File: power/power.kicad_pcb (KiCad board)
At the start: 4 copper layers, 75 x 56 mm, 61 parts, among them J1 GPIO, J10 SCL1, J11 SDA1, J12 SCL2, J13 SDA2, J14 VCC1, J15 GND1, J16 VCC2, J17 GND2, J18 JP_VCC_PWM, J2 PWM_OUT, J3 PWM_IN, J4 JP_EXT, J5 JP_VOLTS, J6 I2C_EXT1, J7 I2C_EXT2, J8 PWM_OUT, J9 JP_VCC_PWM, Q1 D15P05, Q2 BC847C, U2 REF5050IDGK, U3 L78L06_SOT89, U5 TPS56A37RPAR

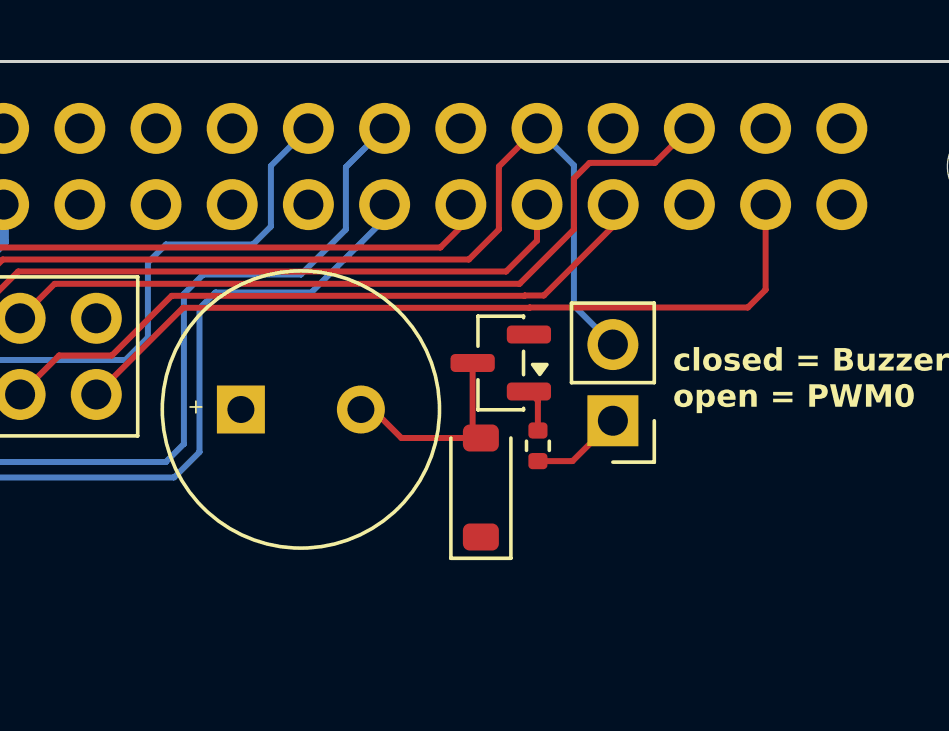
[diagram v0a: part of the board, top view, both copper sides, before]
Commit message: use normally closed solder jumper for buzzer/pwm selection
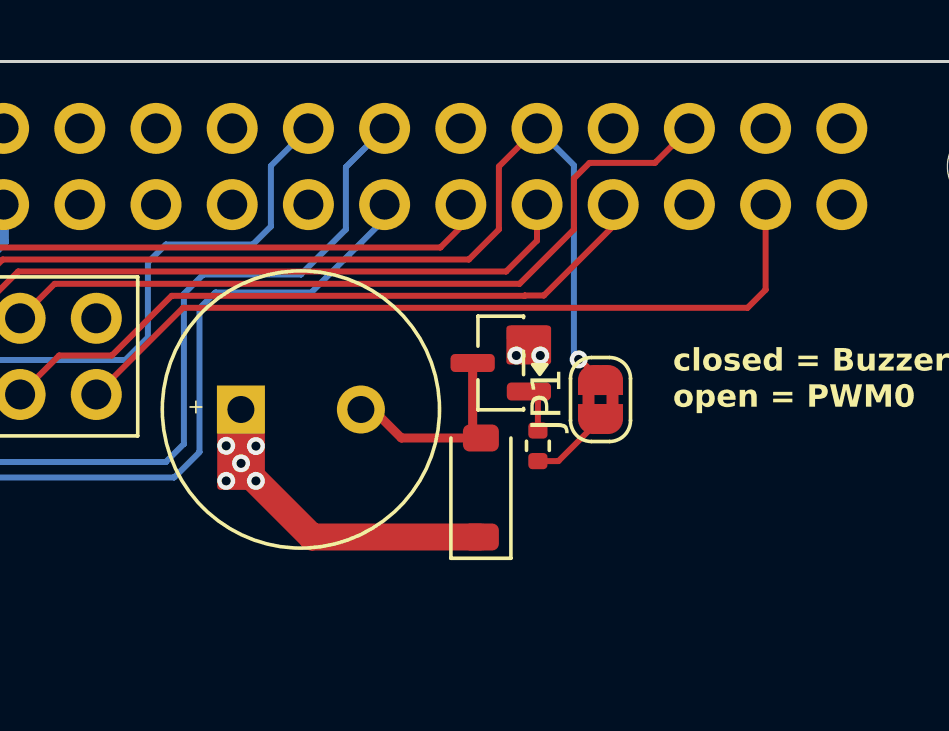
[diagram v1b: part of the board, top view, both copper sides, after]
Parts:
- JP1: footprint Connector_PinHeader_2.54mm:PinHeader_1x02_P2.54mm_Vertical -> Jumper:SolderJumper-2_P1.3mm_Bridged2Bar_RoundedPad1.0x1.5mm
- moved JP1 0.82 mm to (148.6, 55.3), turned to 90 degrees
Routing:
- net +5V: track 26.9 -> 35.1 mm, vias 33 -> 38
- net /GPIO12/PWM0: track 31.9 -> 32.9 mm, vias 0 -> 1
- net GND: vias 78 -> 80

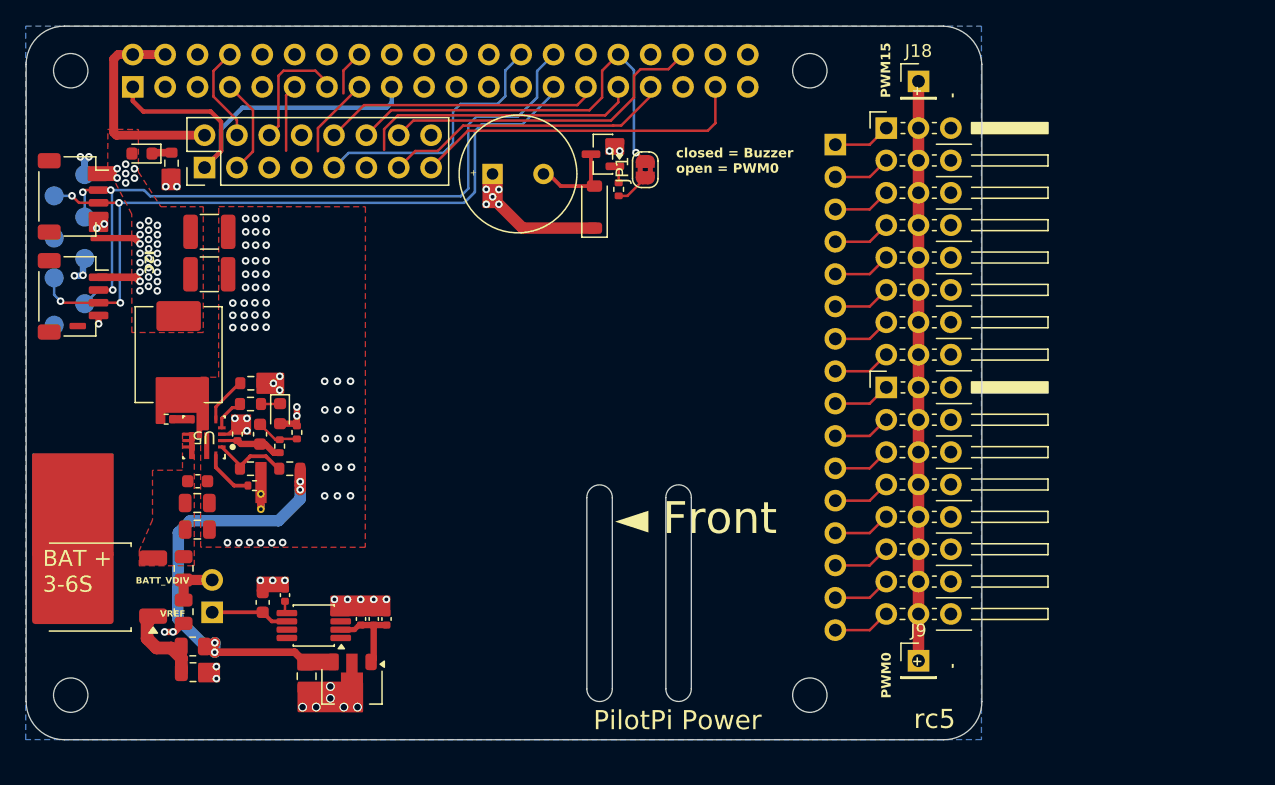
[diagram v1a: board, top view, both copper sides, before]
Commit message: power jumper for i2c extender (default 3V3); preliminary RS485 transceiver
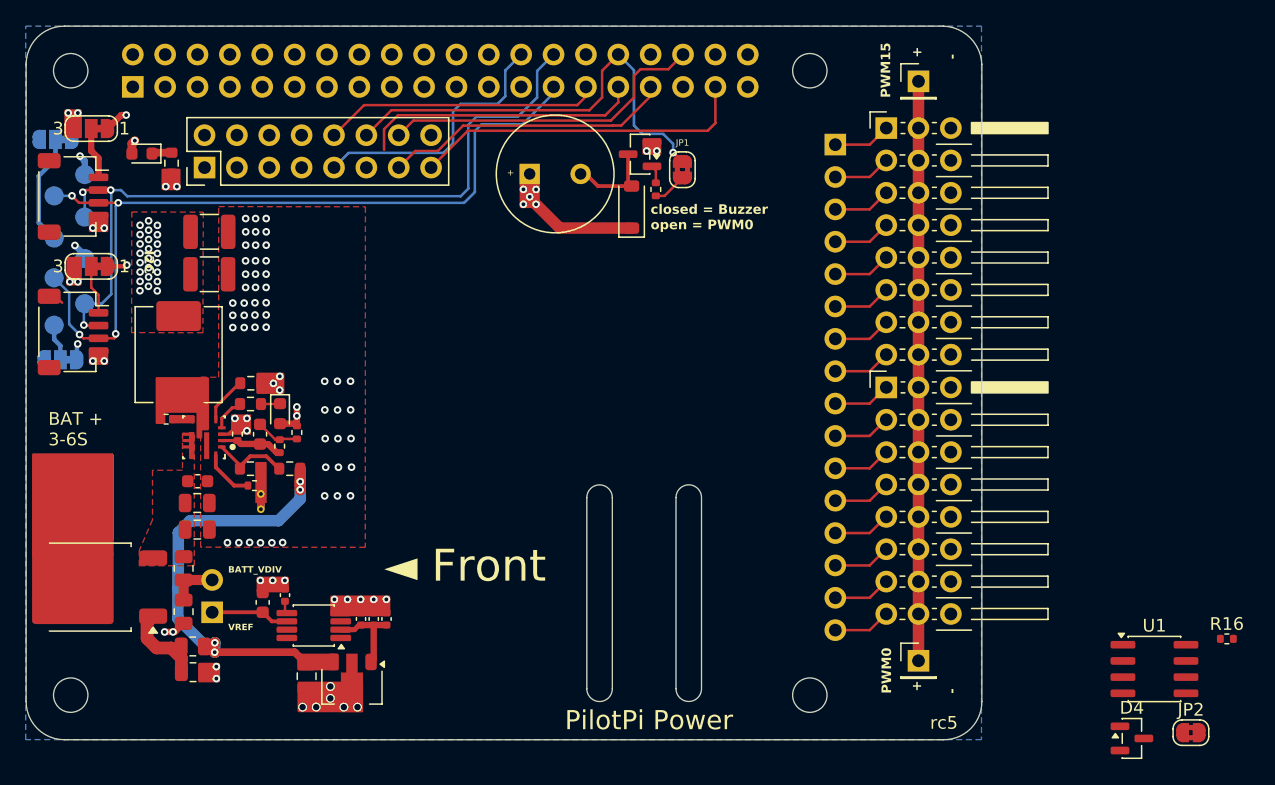
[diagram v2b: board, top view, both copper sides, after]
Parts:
- added D4: SM712_SOT23, Package_TO_SOT_SMD:SOT-23, F.Cu at (186.8, 99.9)
- added J19: Conn_01x01, Connector_Wire:SolderWirePad_1x01_SMD_1.5x3mm, F.Cu at (103.7, 80.5)
- added JP2: JP_RS485_TERM, Jumper:SolderJumper-2_P1.3mm_Bridged2Bar_RoundedPad1.0x1.5mm, F.Cu at (191.4, 99.4)
- added JP_I2C_PWR_3: 5V_OR_3V3, Jumper:SolderJumper-3_P1.3mm_Bridged12_RoundedPad1.0x1.5mm_NumberLabels, F.Cu at (105.1, 62.9)
- added JP_I2C_PWR_4: 5V_OR_3V3, Jumper:SolderJumper-3_P1.3mm_Bridged12_RoundedPad1.0x1.5mm_NumberLabels, F.Cu at (105.1, 52.0)
- added JP_I2C_PWR_5: 5V_OR_3V3, Jumper:SolderJumper-3_P1.3mm_Bridged12_RoundedPad1.0x1.5mm_NumberLabels, B.Cu at (102.7, 70.2)
- added JP_I2C_PWR_6: 5V_OR_3V3, Jumper:SolderJumper-3_P1.3mm_Bridged12_RoundedPad1.0x1.5mm_NumberLabels, B.Cu at (102.3, 52.9)
- added R16: 120Ω ±1%, Resistor_SMD:R_0402_1005Metric, F.Cu at (194.2, 92.1)
- added U1: SP3485EN, Package_SO:SOIC-8_3.9x4.9mm_P1.27mm, F.Cu at (188.5, 94.5)
- moved Q2 2.92 mm to (148.2, 54.0)
- moved BZ1 2.91 mm to (139.5, 55.6)
- moved D3 2.91 mm to (147.5, 58.2)
- moved JP1 2.91 mm to (151.5, 55.3)
- moved R6 2.91 mm to (149.4, 56.8)
- moved J6 2.79 mm to (103.7, 68.0)
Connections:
- J14 pad 1: +5V -> Net-(J14-Pin_1)
- J16 pad 1: +5V -> Net-(J16-Pin_1)
- J4 pad 10: /GPIO5 -> unconnected-(J4-Pin_10-Pad10)
- J4 pad 12: /GPIO12/PWM0 -> unconnected-(J4-Pin_12-Pad12)
- J4 pad 13: /GPIO13/PWM1 -> unconnected-(J4-Pin_13-Pad13)
- J4 pad 14: /GPIO16 -> unconnected-(J4-Pin_14-Pad14)
- J4 pad 15: /GPIO26 -> unconnected-(J4-Pin_15-Pad15)
- J4 pad 3: /GPIO4/GPCLK0 -> unconnected-(J4-Pin_3-Pad3)
- J4 pad 4: /GPIO14/TXD0 -> unconnected-(J4-Pin_4-Pad4)
- J4 pad 6: /GPIO27 -> unconnected-(J4-Pin_6-Pad6)
- J4 pad 9: /GPIO7/SPI0.CE1 -> unconnected-(J4-Pin_9-Pad9)
- J6 pad 1: +5V -> Net-(J6-Pin_1)
- J7 pad 1: +5V -> Net-(J7-Pin_1)
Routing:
- net +3V3: track 31.9 -> 56.4 mm, vias 0 -> 3
- net +5V: track 35.1 -> 12.3 mm, vias 38 -> 36
- net /GPIO27: track 9.31 -> 0.00 mm
- net Net-(J16-Pin_1): track 0.00 -> 8.79 mm
- net /GPIO14/TXD0: track 7.63 -> 0.00 mm
- net /GPIO4/GPCLK0: track 7.60 -> 0.00 mm
- net /GPIO22: track 6.41 -> 0.00 mm
- net /GPIO17: track 5.29 -> 0.00 mm
- net /GPIO0/SDA0: track 61.5 -> 65.6 mm
- net Net-(J7-Pin_1): track 0.00 -> 4.06 mm
- net Net-(J6-Pin_1): track 0.00 -> 3.88 mm
- net /GPIO23: track 3.57 -> 0.00 mm
- net Net-(J14-Pin_1): track 0.00 -> 2.91 mm
- net GND: track 7.55 -> 4.85 mm, vias 80 -> 79
- net /GPIO12/PWM0: track 32.9 -> 35.3 mm
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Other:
- outline, holes or cut-outs redrawn
- board text added: "${CURRENT_DATE}"

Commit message: routing of RS485 transceiver
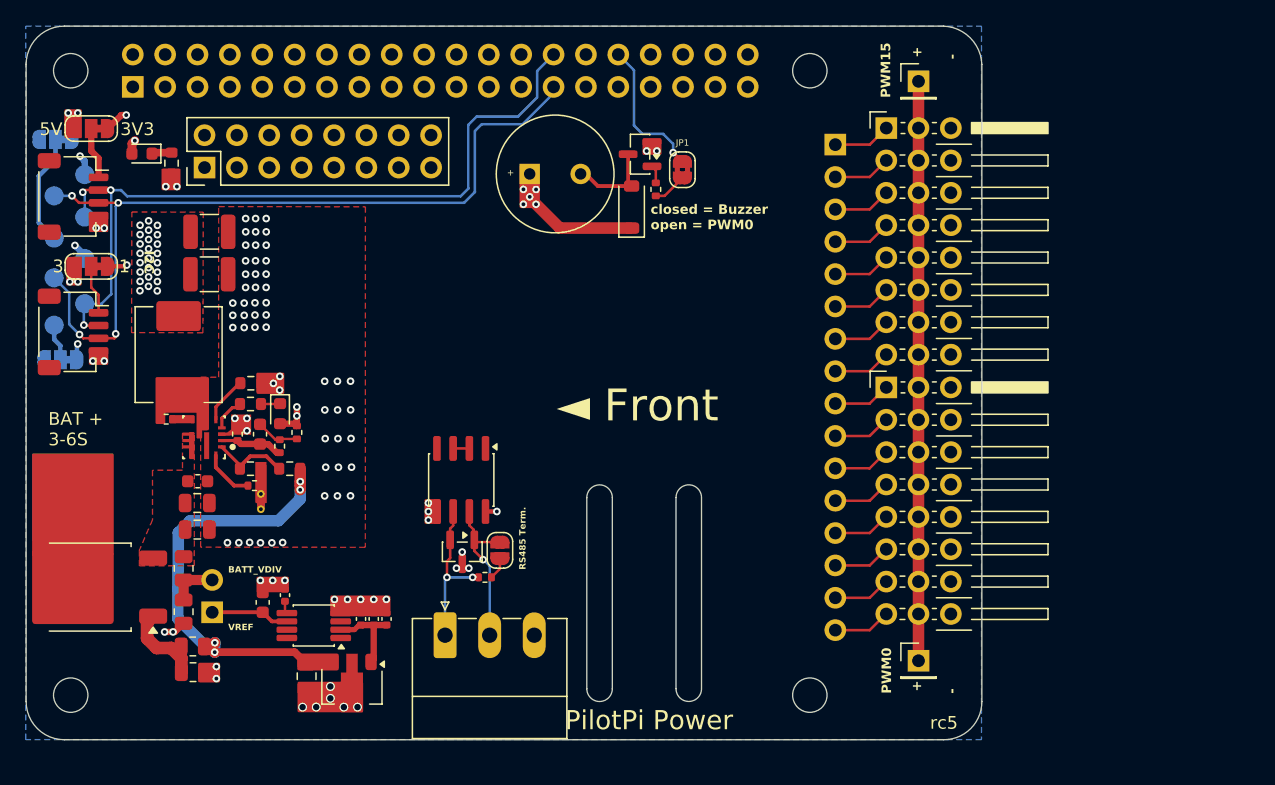
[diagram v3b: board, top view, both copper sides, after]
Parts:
- added J20: CONN_RS485, Connector_Phoenix_MC:PhoenixContact_MC_1,5_3-G-3.5_1x03_P3.50mm_Horizontal, F.Cu at (132.9, 91.8)
- JP2: footprint Jumper:SolderJumper-2_P1.3mm_Bridged2Bar_RoundedPad1.0x1.5mm -> Jumper:SolderJumper-2_P1.3mm_Open_RoundedPad1.0x1.5mm
- moved R16 58.4 mm to (136.0, 87.3)
- moved U1 56.4 mm to (134.1, 79.6), turned to -90 degrees
- moved JP2 56.1 mm to (137.2, 85.1), turned to -90 degrees
- moved D4 54.6 mm to (134.2, 85.2), turned to -90 degrees
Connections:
- D4 pad 1: /RS485/A -> /RS485/B
- D4 pad 2: /RS485/B -> /RS485/A
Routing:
- net +3V3: track 56.4 -> 104.6 mm, vias 3 -> 4
- net /GPIO26: track 26.6 -> 0.00 mm
- net /GPIO16: track 25.9 -> 0.00 mm
- net /GPIO12/PWM0: track 35.3 -> 11.7 mm
- net /GPIO13/PWM1: track 22.1 -> 0.00 mm
- net /GPIO6: track 22.1 -> 0.00 mm
- net /GPIO5: track 21.8 -> 0.00 mm
- net /GPIO7/SPI0.CE1: track 21.0 -> 0.00 mm
- net /RS485/A: track 0.00 -> 12.7 mm, vias 0 -> 2
- net /RS485/B: track 0.00 -> 12.5 mm, vias 0 -> 1
- net Net-(JP2-B): track 0.00 -> 1.74 mm
- net /RS485/RTS: track 0.00 -> 1.27 mm
- net GND: vias 79 -> 85
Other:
- board text added: "RS485 Term."

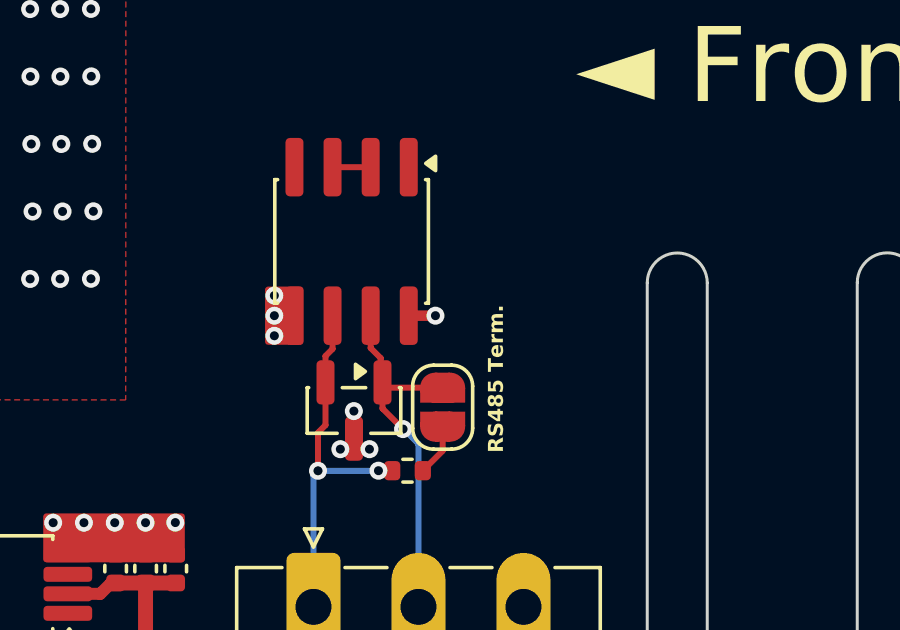
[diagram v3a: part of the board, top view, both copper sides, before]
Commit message: add 100nF to SP3485
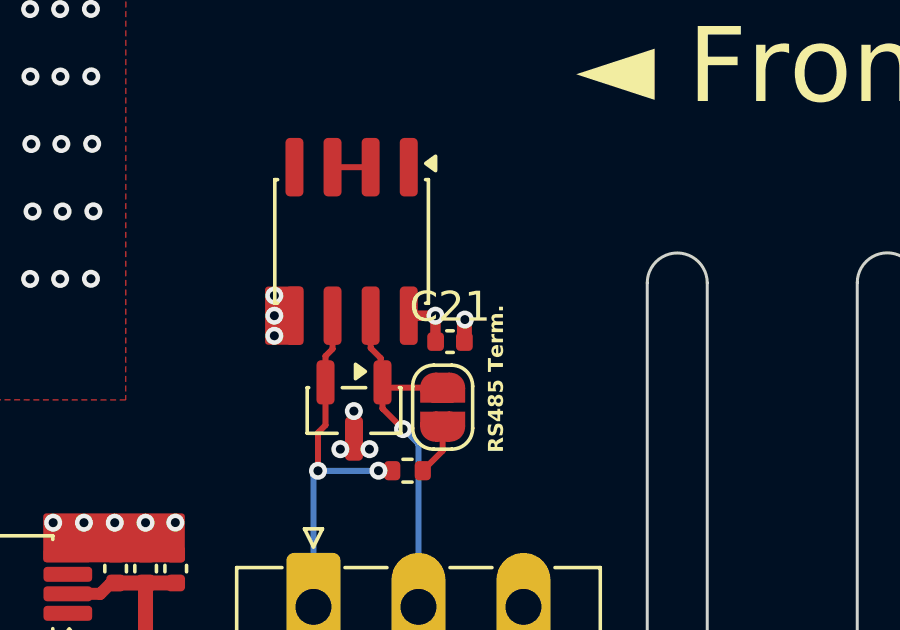
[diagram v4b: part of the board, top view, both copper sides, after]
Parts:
- added C21: 100nF (104) 10% 16V, Capacitor_SMD:C_0402_1005Metric, F.Cu at (137.4, 83.0)
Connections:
- U1 pad 1: /RS485/DO -> /GPIO15/RXD0
- U1 pad 4: /RS485/RI -> /GPIO14/TXD0
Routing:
- net +3V3: track 104.6 -> 105.5 mm
- net GND: track 4.85 -> 5.59 mm, vias 85 -> 86

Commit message: RS485 labels
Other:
- board text added: "A"
- board text added: "B"
- board text added: "RS485"
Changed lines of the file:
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@@
 			(at 3.5 9.2 0)
 			(layer "F.Fab")
+			(hide yes)
 			(effects
 				(font
@@
 		)
 	)
+	(gr_text "A"
+		(at 132.87404 88.91 0)
+		(layer "F.SilkS")
+		(effects
+			(font
+				(size 0.75 0.75)
+				(thickness 0.1875)
+				(bold yes)
+			)
+			(justify bottom)
+		)
+	)
+	(gr_text "B"
+		(at 136.37404 88.91 0)
+		(layer "F.SilkS")
+		(effects
+			(font
+				(size 0.75 0.75)
+				(thickness 0.1875)
+				(bold yes)
+			)
+			(justify bottom)
+		)
+	)
+	(gr_text "RS485"
+		(at 136.37404 99.03 0)
+		(layer "F.SilkS")
+		(effects
+			(font
+				(size 0.75 0.75)
+				(thickness 0.1875)
+				(bold yes)
+			)
+			(justify bottom)
+		)
+	)
+	(gr_text "GND"
+		(at 139.87404 88.91 0)
+		(layer "F.SilkS")
+		(effects
+			(font
+				(size 0.75 0.75)
+				(thickness 0.1875)
+				(bold yes)
+			)
+			(justify bottom)
+		)
+	)
 	(gr_text "BAT +\n3-6S"
 		(at 101.74 77.02 0)
@@
 	)
 	(gr_text "PilotPi Power"
-		(at 142.27 99.356212 0)
+		(at 144.07 99.356212 0)
 		(layer "F.SilkS")
 		(effects

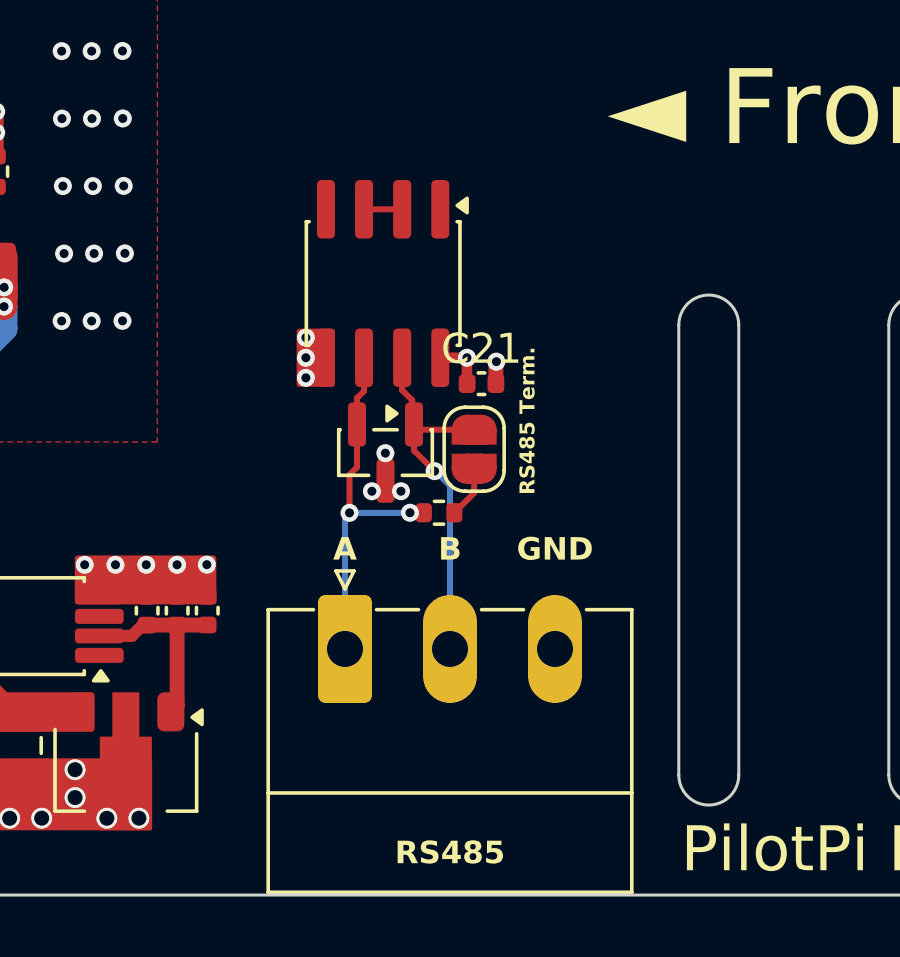
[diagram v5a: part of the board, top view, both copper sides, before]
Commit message: move SP3485 to sensors board and connect to UART port A
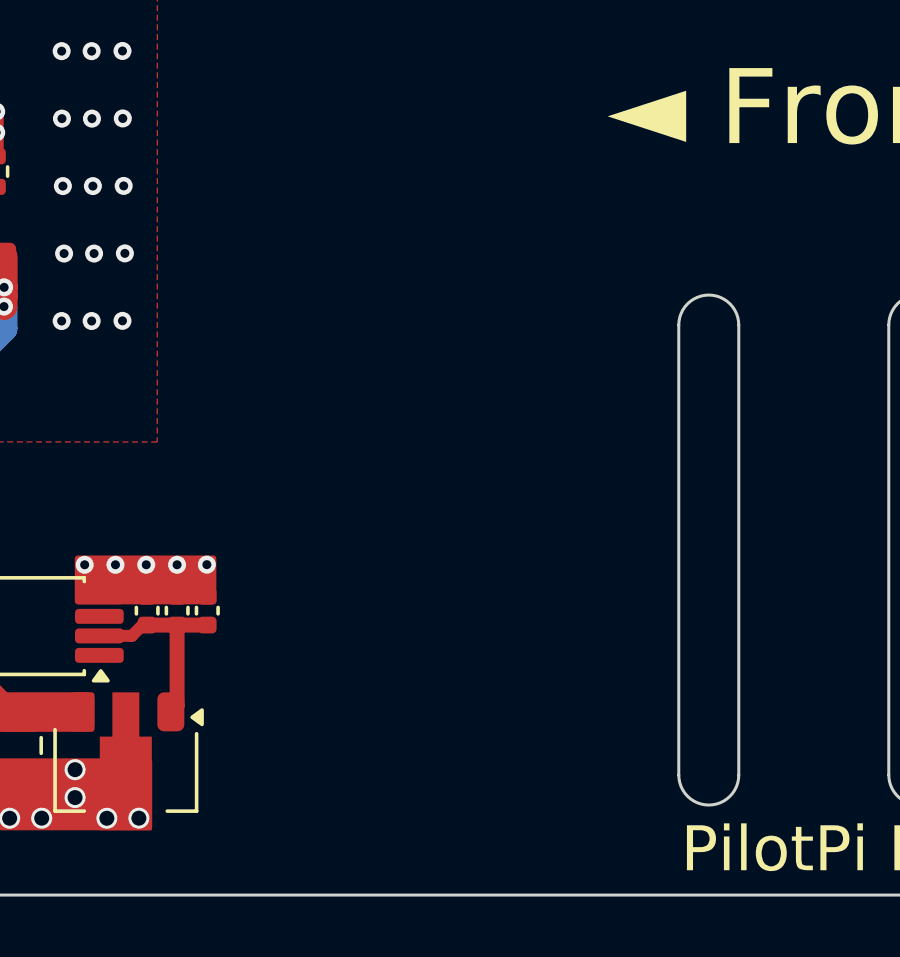
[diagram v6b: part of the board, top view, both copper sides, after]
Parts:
- removed C21: 100nF (104) 10% 16V, Capacitor_SMD:C_0402_1005Metric
- removed D4: SM712_SOT23, Package_TO_SOT_SMD:SOT-23
- removed J20: CONN_RS485, Connector_Phoenix_MC:PhoenixContact_MC_1,5_3-G-3.5_1x03_P3.50mm_Horizontal
- removed JP2: JP_RS485_TERM, Jumper:SolderJumper-2_P1.3mm_Open_RoundedPad1.0x1.5mm
- removed R16: 120Ω ±1%, Resistor_SMD:R_0402_1005Metric
- removed U1: SP3485EN, Package_SO:SOIC-8_3.9x4.9mm_P1.27mm
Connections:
- net /GPIO17 renamed /GPIO17/RTS0
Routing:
- net +3V3: track 105.5 -> 56.4 mm, vias 4 -> 3
- net /RS485/A: track 12.7 -> 0.00 mm, vias 2 -> 0
- net /RS485/B: track 12.5 -> 0.00 mm, vias 1 -> 0
- net Net-(JP2-B): track 1.74 -> 0.00 mm
- net /RS485/RTS: track 1.27 -> 0.00 mm
- net GND: track 5.59 -> 4.85 mm, vias 86 -> 79
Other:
- board text removed: "A"
- board text removed: "B"
- board text removed: "RS485"
- board text removed: "RS485 Term."
